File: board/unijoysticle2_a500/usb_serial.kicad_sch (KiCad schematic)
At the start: 12 parts, among them J1 USB_B_Micro, U2 AMS1117-3.3, U3 CH340C

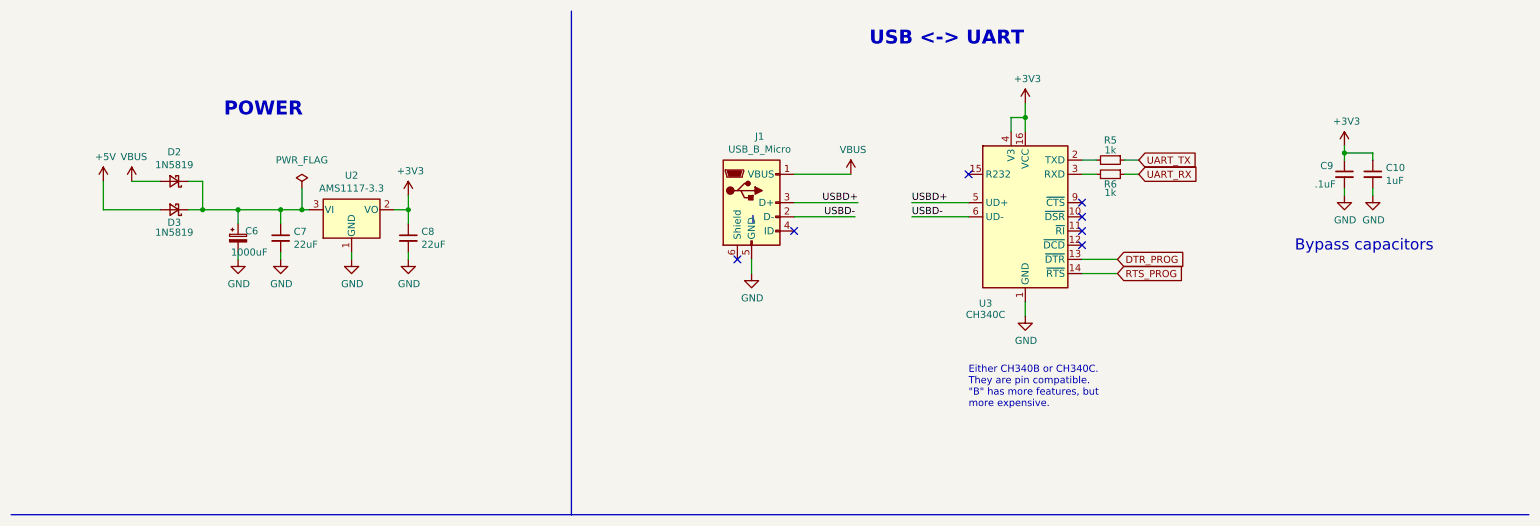
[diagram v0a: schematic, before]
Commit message: uni a500+: remove LSCS column
Values were outdated
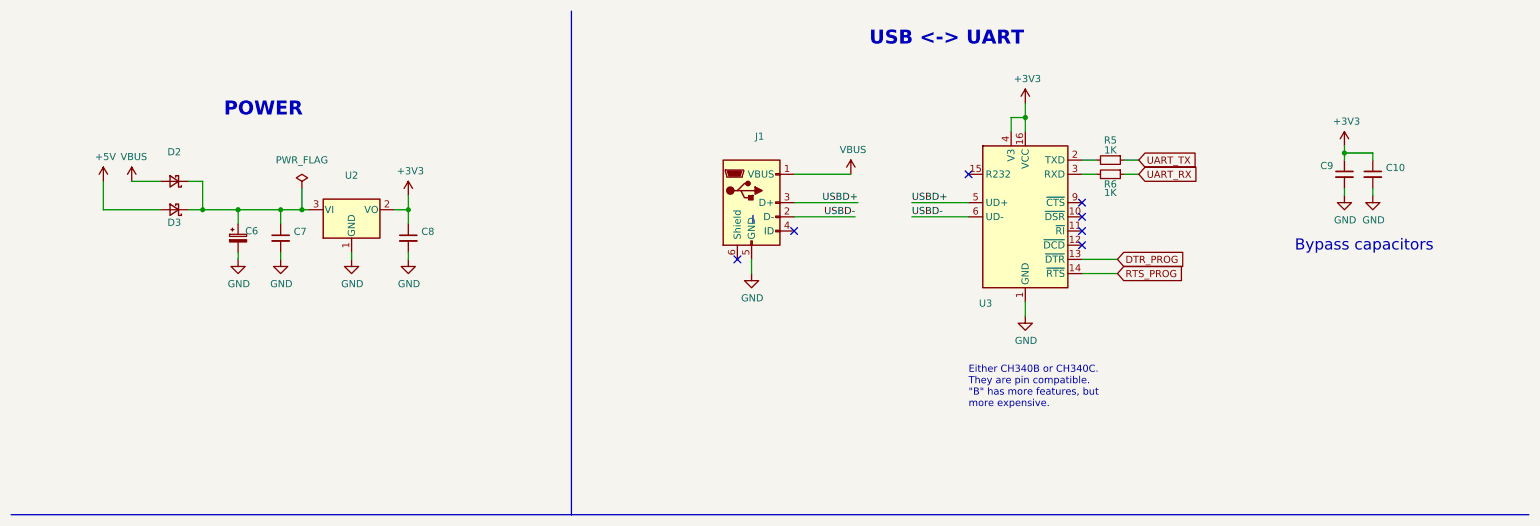
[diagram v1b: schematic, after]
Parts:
- C10: value 1uF -> (none); footprint Capacitor_SMD:C_0805_2012Metric_Pad1.18x1.45mm_HandSolder -> (none); LCSC C28323 -> (none)
- C6: value 1000uF -> (none); footprint Capacitor_SMD:CP_Elec_10x10 -> (none)
- C7, C8: value 22uF -> (none); footprint Capacitor_SMD:C_0805_2012Metric_Pad1.18x1.45mm_HandSolder -> (none); LCSC C45783 -> (none)
- C9: value .1uF -> (none); footprint Capacitor_SMD:C_0805_2012Metric_Pad1.18x1.45mm_HandSolder -> (none); LCSC C49678 -> (none)
- D2, D3: value 1N5819 -> (none); footprint Diode_SMD:D_SOD-123 -> (none); LCSC C8598 -> (none)
- J1: value USB_B_Micro -> (none); footprint Connector_USB:USB_Micro-B_Amphenol_10118194_Horizontal -> (none); LCSC C132563 -> (none)
- R5, R6: value 1k -> 1K; footprint Resistor_SMD:R_0805_2012Metric_Pad1.20x1.40mm_HandSolder -> (none); LCSC C17513 -> (none)
- U2: value AMS1117-3.3 -> (none); footprint Package_TO_SOT_SMD:SOT-223-3_TabPin2 -> (none); LCSC C6186 -> (none)
- U3: value CH340C -> (none); footprint Package_SO:SOIC-16_3.9x9.9mm_P1.27mm -> (none); LCSC C84681 -> (none)
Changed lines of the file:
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@@
       (effects (font (size 1.27 1.27)) (justify left))
     )
-    (property "Value" "22uF" (id 1) (at 63.2968 54.483 0)
-      (effects (font (size 1.27 1.27)) (justify left))
-    )
-    (property "Footprint" "Capacitor_SMD:C_0805_2012Metric_Pad1.18x1.45mm_HandSolder" (id 2) (at 60.96 53.34 0)
+    (property "Value" "" (id 1) (at 63.2968 54.483 0)
+      (effects (font (size 1.27 1.27)) (justify left))
+    )
+    (property "Footprint" "" (id 2) (at 60.96 53.34 0)
       (effects (font (size 1.27 1.27)) hide)
     )
@@
       (effects (font (size 1.27 1.27)) hide)
     )
-    (property "LCSC" "C45783" (id 4) (at 60.96 53.34 0)
+    (property "LCSC" "" (id 4) (at 60.96 53.34 0)
       (effects (font (size 1.27 1.27)) hide)
     )
@@
       (effects (font (size 1.27 1.27)) (justify left))
     )
-    (property "Value" "22uF" (id 1) (at 86.1568 54.483 0)
-      (effects (font (size 1.27 1.27)) (justify left))
-    )
-    (property "Footprint" "Capacitor_SMD:C_0805_2012Metric_Pad1.18x1.45mm_HandSolder" (id 2) (at 83.82 53.34 0)
+    (property "Value" "" (id 1) (at 86.1568 54.483 0)
+      (effects (font (size 1.27 1.27)) (justify left))
+    )
+    (property "Footprint" "" (id 2) (at 83.82 53.34 0)
       (effects (font (size 1.27 1.27)) hide)
     )
@@
       (effects (font (size 1.27 1.27)) hide)
     )
-    (property "LCSC" "C45783" (id 4) (at 83.82 53.34 0)
+    (property "LCSC" "" (id 4) (at 83.82 53.34 0)
       (effects (font (size 1.27 1.27)) hide)
     )
@@
     (in_bom yes) (on_board yes)
     (property "Reference" "U2" (id 0) (at 73.66 42.1132 0))
-    (property "Value" "AMS1117-3.3" (id 1) (at 73.66 44.4246 0))
-    (property "Footprint" "Package_TO_SOT_SMD:SOT-223-3_TabPin2" (id 2) (at 73.66 43.18 0)
+    (property "Value" "" (id 1) (at 73.66 44.4246 0))
+    (property "Footprint" "" (id 2) (at 73.66 43.18 0)
       (effects (font (size 1.27 1.27)) hide)
     )
@@
       (effects (font (size 1.27 1.27)) hide)
     )
-    (property "LCSC" "C6186" (id 4) (at 73.66 48.26 0)
+    (property "LCSC" "" (id 4) (at 73.66 48.26 0)
       (effects (font (size 1.27 1.27)) hide)
     )
@@
     (in_bom yes) (on_board yes)
     (property "Reference" "U3" (id 0) (at 187.198 65.024 0))
-    (property "Value" "CH340C" (id 1) (at 187.198 67.056 0))
-    (property "Footprint" "Package_SO:SOIC-16_3.9x9.9mm_P1.27mm" (id 2) (at 195.58 63.5 0)
+    (property "Value" "" (id 1) (at 187.198 67.056 0))
+    (property "Footprint" "" (id 2) (at 195.58 63.5 0)
       (effects (font (size 1.27 1.27)) (justify left) hide)
     )
@@
       (effects (font (size 1.27 1.27)) hide)
     )
-    (property "LCSC" "C84681" (id 4) (at 194.31 49.53 0)
+    (property "LCSC" "" (id 4) (at 194.31 49.53 0)
       (effects (font (size 1.27 1.27)) hide)
     )
@@
       (effects (font (size 1.27 1.27)) (justify left))
     )
-    (property "Value" ".1uF" (id 1) (at 246.126 43.688 0)
-      (effects (font (size 1.27 1.27)) (justify left))
-    )
-    (property "Footprint" "Capacitor_SMD:C_0805_2012Metric_Pad1.18x1.45mm_HandSolder" (id 2) (at 251.46 41.91 0)
+    (property "Value" "" (id 1) (at 246.126 43.688 0)
+      (effects (font (size 1.27 1.27)) (justify left))
+    )
+    (property "Footprint" "" (id 2) (at 251.46 41.91 0)
       (effects (font (size 1.27 1.27)) hide)
     )
@@
       (effects (font (size 1.27 1.27)) hide)
     )
-    (property "LCSC" "C49678" (id 4) (at 251.46 41.91 0)
+    (property "LCSC" "" (id 4) (at 251.46 41.91 0)
       (effects (font (size 1.27 1.27)) hide)
     )
@@
     (in_bom yes) (on_board yes)
     (property "Reference" "R5" (id 0) (at 209.55 35.814 90))
-    (property "Value" "1k" (id 1) (at 209.55 37.592 90))
-    (property "Footprint" "Resistor_SMD:R_0805_2012Metric_Pad1.20x1.40mm_HandSolder" (id 2) (at 209.55 39.37 0)
+    (property "Value" "1K" (id 1) (at 209.55 37.592 90))
+    (property "Footprint" "" (id 2) (at 209.55 39.37 0)
       (effects (font (size 1.27 1.27)) hide)
     )
@@
       (effects (font (size 1.27 1.27)) hide)
     )
-    (property "LCSC" "C17513" (id 4) (at 209.55 39.37 90)
+    (property "LCSC" "" (id 4) (at 209.55 39.37 90)
       (effects (font (size 1.27 1.27)) hide)
     )
@@
       (effects (font (size 1.27 1.27)) (justify left))
     )
-    (property "Value" "1uF" (id 1) (at 258.8768 43.053 0)
-      (effects (font (size 1.27 1.27)) (justify left))
-    )
-    (property "Footprint" "Capacitor_SMD:C_0805_2012Metric_Pad1.18x1.45mm_HandSolder" (id 2) (at 256.54 41.91 0)
+    (property "Value" "" (id 1) (at 258.8768 43.053 0)
+      (effects (font (size 1.27 1.27)) (justify left))
+    )
+    (property "Footprint" "" (id 2) (at 256.54 41.91 0)
       (effects (font (size 1.27 1.27)) hide)
     )
@@
       (effects (font (size 1.27 1.27)) hide)
     )
-    (property "LCSC" "C28323" (id 4) (at 256.54 41.91 0)
+    (property "LCSC" "" (id 4) (at 256.54 41.91 0)
       (effects (font (size 1.27 1.27)) hide)
     )
@@
     (in_bom yes) (on_board yes)
     (property "Reference" "R6" (id 0) (at 209.55 43.688 90))
-    (property "Value" "1k" (id 1) (at 209.55 45.212 90))
-    (property "Footprint" "Resistor_SMD:R_0805_2012Metric_Pad1.20x1.40mm_HandSolder" (id 2) (at 209.55 41.91 0)
+    (property "Value" "1K" (id 1) (at 209.55 45.212 90))
+    (property "Footprint" "" (id 2) (at 209.55 41.91 0)
       (effects (font (size 1.27 1.27)) hide)
     )
@@
       (effects (font (size 1.27 1.27)) hide)
     )
-    (property "LCSC" "C17513" (id 4) (at 209.55 41.91 90)
+    (property "LCSC" "" (id 4) (at 209.55 41.91 90)
       (effects (font (size 1.27 1.27)) hide)
     )
@@
     (in_bom yes) (on_board yes)
     (property "Reference" "D2" (id 0) (at 41.91 37.9222 0))
-    (property "Value" "1N5819" (id 1) (at 41.91 40.2336 0))
-    (property "Footprint" "Diode_SMD:D_SOD-123" (id 2) (at 41.91 43.18 90)
+    (property "Value" "" (id 1) (at 41.91 40.2336 0))
+    (property "Footprint" "" (id 2) (at 41.91 43.18 90)
       (effects (font (size 1.27 1.27)) hide)
     )
@@
       (effects (font (size 1.27 1.27)) hide)
     )
-    (property "LCSC" "C8598" (id 4) (at 41.91 43.18 0)
+    (property "LCSC" "" (id 4) (at 41.91 43.18 0)
       (effects (font (size 1.27 1.27)) hide)
     )
@@
     (in_bom yes) (on_board yes)
     (property "Reference" "D3" (id 0) (at 41.91 50.546 0))
-    (property "Value" "1N5819" (id 1) (at 41.91 52.324 0))
-    (property "Footprint" "Diode_SMD:D_SOD-123" (id 2) (at 41.91 48.26 90)
+    (property "Value" "" (id 1) (at 41.91 52.324 0))
+    (property "Footprint" "" (id 2) (at 41.91 48.26 90)
       (effects (font (size 1.27 1.27)) hide)
     )
@@
       (effects (font (size 1.27 1.27)) hide)
     )
-    (property "LCSC" "C8598" (id 4) (at 41.91 48.26 0)
+    (property "LCSC" "" (id 4) (at 41.91 48.26 0)
       (effects (font (size 1.27 1.27)) hide)
     )
@@
     (in_bom yes) (on_board yes)
     (property "Reference" "J1" (id 0) (at 146.7358 35.1282 0))
-    (property "Value" "USB_B_Micro" (id 1) (at 146.7358 37.4396 0))
-    (property "Footprint" "Connector_USB:USB_Micro-B_Amphenol_10118194_Horizontal" (id 2) (at 149.098 48.26 0)
+    (property "Value" "" (id 1) (at 146.7358 37.4396 0))
+    (property "Footprint" "" (id 2) (at 149.098 48.26 0)
       (effects (font (size 1.27 1.27)) hide)
     )
@@
       (effects (font (size 1.27 1.27)) hide)
     )
-    (property "LCSC" "C132563" (id 4) (at 145.288 46.99 0)
+    (property "LCSC" "" (id 4) (at 145.288 46.99 0)
       (effects (font (size 1.27 1.27)) hide)
     )
@@
       (effects (font (size 1.27 1.27)) (justify left))
     )
-    (property "Value" "1000uF" (id 1) (at 52.07 55.88 0)
-      (effects (font (size 1.27 1.27)) (justify left))
-    )
-    (property "Footprint" "Capacitor_SMD:CP_Elec_10x10" (id 2) (at 53.34 53.34 0)
-      (effects (font (size 1.27 1.27)) hide)
-    )
+    (property "Value" "" (id 1) (at 52.07 55.88 0)
+      (effects (font (size 1.27 1.27)) (justify left))
+    )
+    (property "Footprint" "" (id 2) (at 53.34 53.34 0)
+      (effects (font (size 1.27 1.27)) hide)
+    )

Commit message: Uni 2 A500 Rev B:
- Cap 1500uF instead of 1000uF
- Use Resister 0 (R15) instead of JP2. Back resistor for JP2 2.2K
- LED resistors to be 2.2K
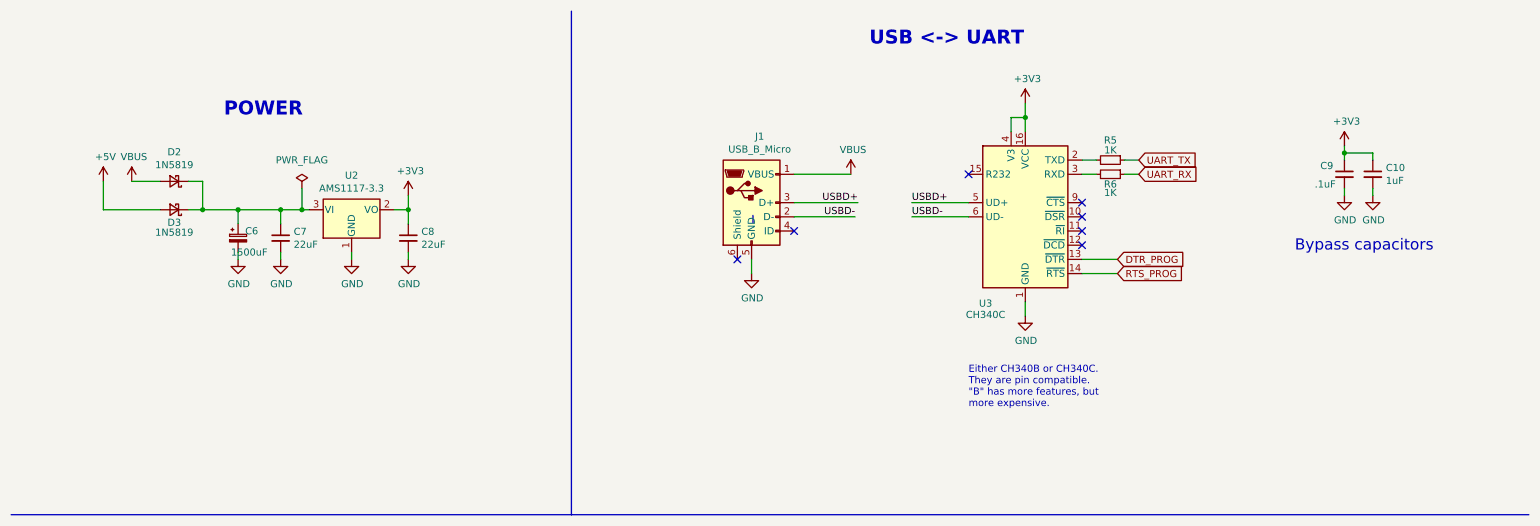
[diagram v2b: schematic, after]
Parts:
- C10: value (none) -> 1uF; footprint (none) -> Capacitor_SMD:C_0805_2012Metric_Pad1.18x1.45mm_HandSolder
- C6: value (none) -> 1500uF; footprint (none) -> Capacitor_SMD:CP_Elec_10x10
- C7, C8: value (none) -> 22uF; footprint (none) -> Capacitor_SMD:C_0805_2012Metric_Pad1.18x1.45mm_HandSolder
- C9: value (none) -> .1uF; footprint (none) -> Capacitor_SMD:C_0805_2012Metric_Pad1.18x1.45mm_HandSolder
- D2, D3: value (none) -> 1N5819; footprint (none) -> Diode_SMD:D_SOD-123
- J1: value (none) -> USB_B_Micro; footprint (none) -> Connector_USB:USB_Micro-B_Amphenol_10118194_Horizontal
- R5, R6: footprint (none) -> Resistor_SMD:R_0805_2012Metric_Pad1.20x1.40mm_HandSolder
- U2: value (none) -> AMS1117-3.3; footprint (none) -> Package_TO_SOT_SMD:SOT-223-3_TabPin2
- U3: value (none) -> CH340C; footprint (none) -> Package_SO:SOIC-16_3.9x9.9mm_P1.27mm
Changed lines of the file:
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@@
   (title_block
     (title "Unijoysticle 2 A500")
-    (date "2022-04-25")
-    (rev "A")
+    (date "2022-05-15")
+    (rev "B")
     (company "Retro Moe")
   )
@@
       (effects (font (size 1.27 1.27)) (justify left))
     )
-    (property "Value" "" (id 1) (at 63.2968 54.483 0)
-      (effects (font (size 1.27 1.27)) (justify left))
-    )
-    (property "Footprint" "" (id 2) (at 60.96 53.34 0)
+    (property "Value" "22uF" (id 1) (at 63.2968 54.483 0)
+      (effects (font (size 1.27 1.27)) (justify left))
+    )
+    (property "Footprint" "Capacitor_SMD:C_0805_2012Metric_Pad1.18x1.45mm_HandSolder" (id 2) (at 60.96 53.34 0)
       (effects (font (size 1.27 1.27)) hide)
     )
@@
       (effects (font (size 1.27 1.27)) (justify left))
     )
-    (property "Value" "" (id 1) (at 86.1568 54.483 0)
-      (effects (font (size 1.27 1.27)) (justify left))
-    )
-    (property "Footprint" "" (id 2) (at 83.82 53.34 0)
+    (property "Value" "22uF" (id 1) (at 86.1568 54.483 0)
+      (effects (font (size 1.27 1.27)) (justify left))
+    )
+    (property "Footprint" "Capacitor_SMD:C_0805_2012Metric_Pad1.18x1.45mm_HandSolder" (id 2) (at 83.82 53.34 0)
       (effects (font (size 1.27 1.27)) hide)
     )
@@
     (in_bom yes) (on_board yes)
     (property "Reference" "U2" (id 0) (at 73.66 42.1132 0))
-    (property "Value" "" (id 1) (at 73.66 44.4246 0))
-    (property "Footprint" "" (id 2) (at 73.66 43.18 0)
+    (property "Value" "AMS1117-3.3" (id 1) (at 73.66 44.4246 0))
+    (property "Footprint" "Package_TO_SOT_SMD:SOT-223-3_TabPin2" (id 2) (at 73.66 43.18 0)
       (effects (font (size 1.27 1.27)) hide)
     )
@@
     (in_bom yes) (on_board yes)
     (property "Reference" "U3" (id 0) (at 187.198 65.024 0))
-    (property "Value" "" (id 1) (at 187.198 67.056 0))
-    (property "Footprint" "" (id 2) (at 195.58 63.5 0)
+    (property "Value" "CH340C" (id 1) (at 187.198 67.056 0))
+    (property "Footprint" "Package_SO:SOIC-16_3.9x9.9mm_P1.27mm" (id 2) (at 195.58 63.5 0)
       (effects (font (size 1.27 1.27)) (justify left) hide)
     )
@@
       (effects (font (size 1.27 1.27)) (justify left))
     )
-    (property "Value" "" (id 1) (at 246.126 43.688 0)
-      (effects (font (size 1.27 1.27)) (justify left))
-    )
-    (property "Footprint" "" (id 2) (at 251.46 41.91 0)
+    (property "Value" ".1uF" (id 1) (at 246.126 43.688 0)
+      (effects (font (size 1.27 1.27)) (justify left))
+    )
+    (property "Footprint" "Capacitor_SMD:C_0805_2012Metric_Pad1.18x1.45mm_HandSolder" (id 2) (at 251.46 41.91 0)
       (effects (font (size 1.27 1.27)) hide)
     )
@@
     (property "Reference" "R5" (id 0) (at 209.55 35.814 90))
     (property "Value" "1K" (id 1) (at 209.55 37.592 90))
-    (property "Footprint" "" (id 2) (at 209.55 39.37 0)
+    (property "Footprint" "Resistor_SMD:R_0805_2012Metric_Pad1.20x1.40mm_HandSolder" (id 2) (at 209.55 39.37 0)
       (effects (font (size 1.27 1.27)) hide)
     )
@@
       (effects (font (size 1.27 1.27)) (justify left))
     )
-    (property "Value" "" (id 1) (at 258.8768 43.053 0)
-      (effects (font (size 1.27 1.27)) (justify left))
-    )
-    (property "Footprint" "" (id 2) (at 256.54 41.91 0)
+    (property "Value" "1uF" (id 1) (at 258.8768 43.053 0)
+      (effects (font (size 1.27 1.27)) (justify left))
+    )
+    (property "Footprint" "Capacitor_SMD:C_0805_2012Metric_Pad1.18x1.45mm_HandSolder" (id 2) (at 256.54 41.91 0)
       (effects (font (size 1.27 1.27)) hide)
     )
@@
     (property "Reference" "R6" (id 0) (at 209.55 43.688 90))
     (property "Value" "1K" (id 1) (at 209.55 45.212 90))
-    (property "Footprint" "" (id 2) (at 209.55 41.91 0)
+    (property "Footprint" "Resistor_SMD:R_0805_2012Metric_Pad1.20x1.40mm_HandSolder" (id 2) (at 209.55 41.91 0)
       (effects (font (size 1.27 1.27)) hide)
     )
@@
     (in_bom yes) (on_board yes)
     (property "Reference" "D2" (id 0) (at 41.91 37.9222 0))
-    (property "Value" "" (id 1) (at 41.91 40.2336 0))
-    (property "Footprint" "" (id 2) (at 41.91 43.18 90)
+    (property "Value" "1N5819" (id 1) (at 41.91 40.2336 0))
+    (property "Footprint" "Diode_SMD:D_SOD-123" (id 2) (at 41.91 43.18 90)
       (effects (font (size 1.27 1.27)) hide)
     )
@@
     (in_bom yes) (on_board yes)
     (property "Reference" "D3" (id 0) (at 41.91 50.546 0))
-    (property "Value" "" (id 1) (at 41.91 52.324 0))
-    (property "Footprint" "" (id 2) (at 41.91 48.26 90)
+    (property "Value" "1N5819" (id 1) (at 41.91 52.324 0))
+    (property "Footprint" "Diode_SMD:D_SOD-123" (id 2) (at 41.91 48.26 90)
       (effects (font (size 1.27 1.27)) hide)
     )
@@
     (in_bom yes) (on_board yes)
     (property "Reference" "J1" (id 0) (at 146.7358 35.1282 0))
-    (property "Value" "" (id 1) (at 146.7358 37.4396 0))
-    (property "Footprint" "" (id 2) (at 149.098 48.26 0)
+    (property "Value" "USB_B_Micro" (id 1) (at 146.7358 37.4396 0))
+    (property "Footprint" "Connector_USB:USB_Micro-B_Amphenol_10118194_Horizontal" (id 2) (at 149.098 48.26 0)
       (effects (font (size 1.27 1.27)) hide)
     )
@@
       (effects (font (size 1.27 1.27)) (justify left))
     )
-    (property "Value" "" (id 1) (at 52.07 55.88 0)
-      (effects (font (size 1.27 1.27)) (justify left))
-    )
-    (property "Footprint" "" (id 2) (at 53.34 53.34 0)
-      (effects (font (size 1.27 1.27)) hide)
-    )
+    (property "Value" "1500uF" (id 1) (at 52.07 55.88 0)
+      (effects (font (size 1.27 1.27)) (justify left))
+    )
+    (property "Footprint" "Capacitor_SMD:CP_Elec_10x10" (id 2) (at 53.34 53.34 0)
+      (effects (font (size 1.27 1.27)) hide)
+    )
